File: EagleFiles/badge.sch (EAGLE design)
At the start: 8 parts, among them Q1 16MHz, U1 ATMEGA328P_TQFP

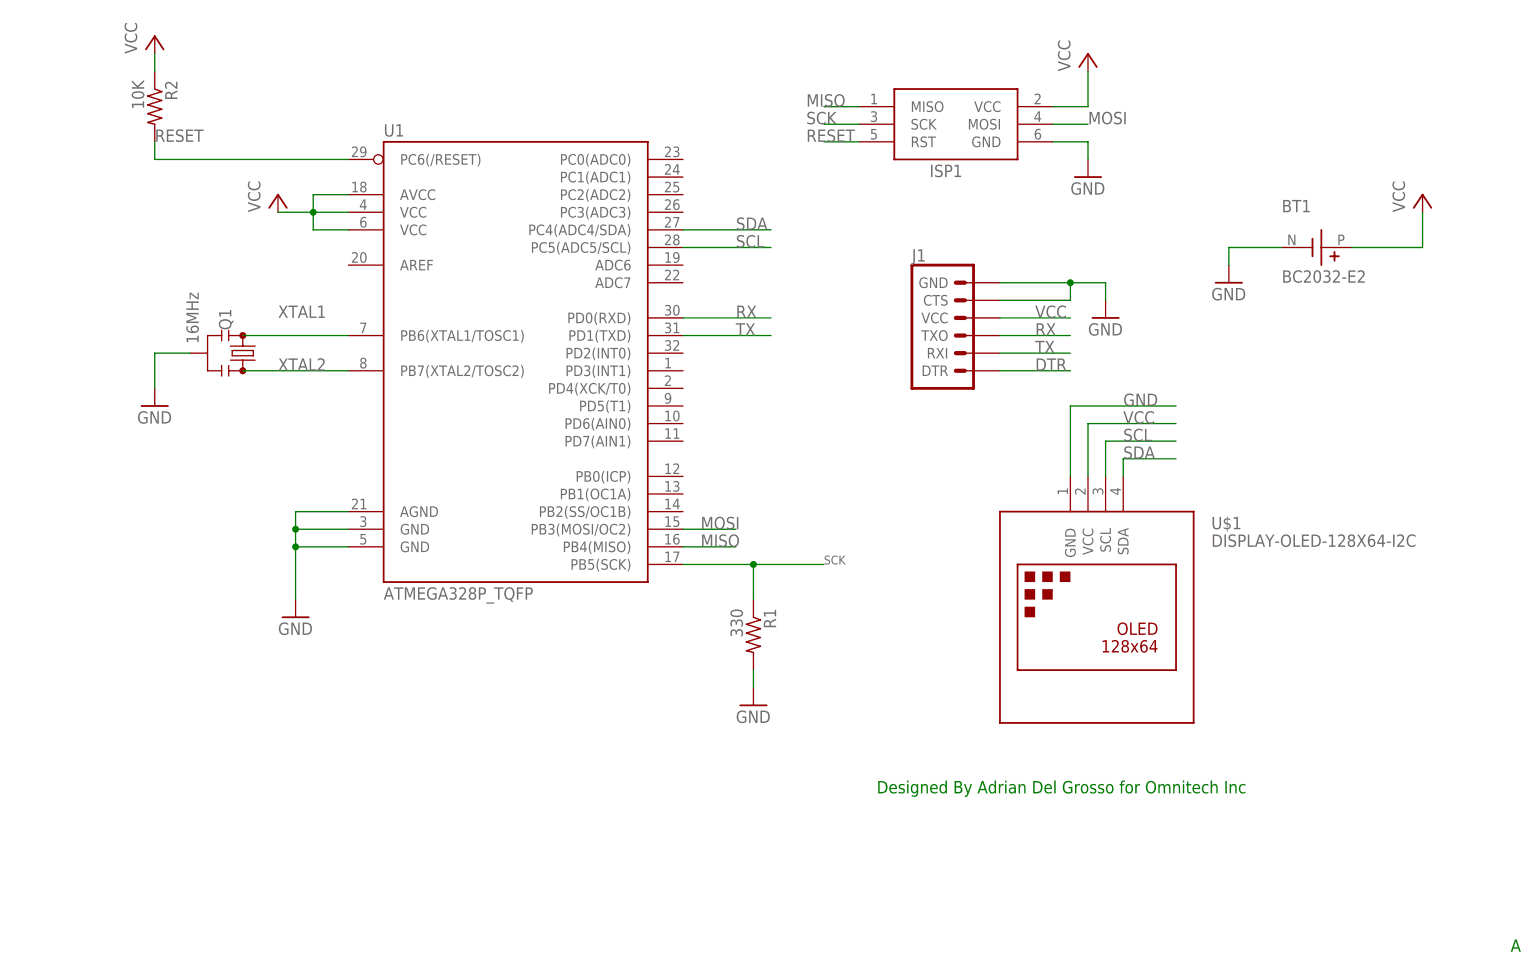
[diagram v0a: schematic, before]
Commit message: Added screen documentation, updated Eagle Files, added starter Arduino sketch
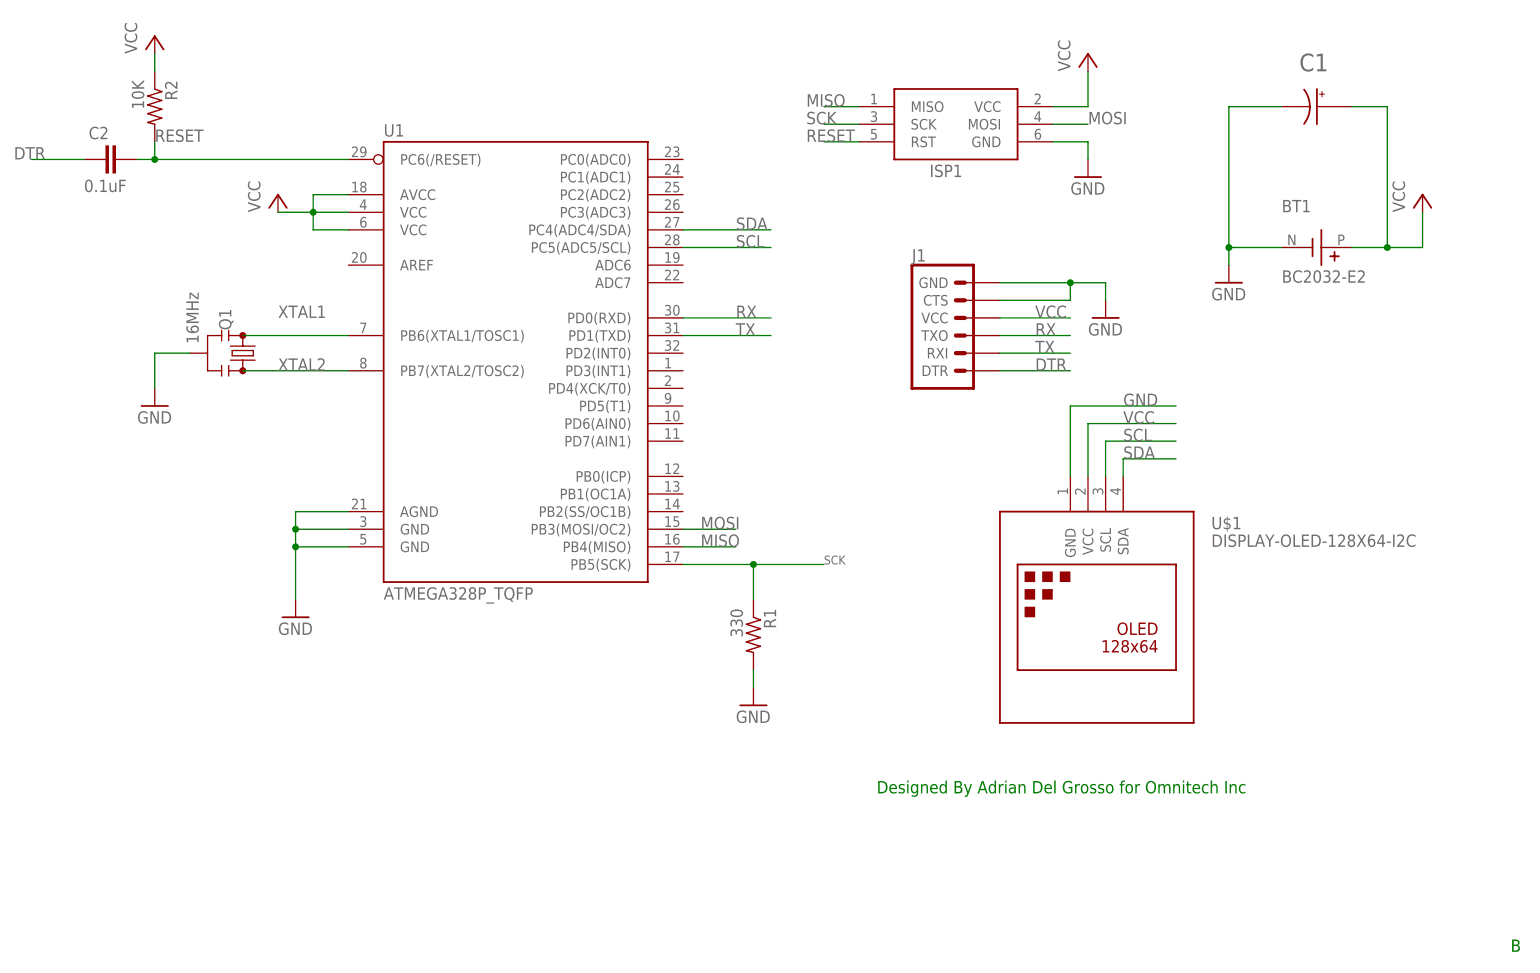
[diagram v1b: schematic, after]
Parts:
- added C1: RNE1C101MDS1PX, RNE1C101MDS1PX:RNE1C101MDS1PX
- added C2: 0.1uF, SparkFun-Capacitors:0.1UF-0402-16V-10%
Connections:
- net DTR: now also C2.1
- net GND: now also C1.N
- net RESET: now also C2.2
- net VCC: now also C1.P
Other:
- note added: "B"
- note removed: "A"
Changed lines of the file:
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@@
 <part name="GND6" library="supply1" library_urn="urn:adsk.eagle:library:371" deviceset="GND" device=""/>
 <part name="P+4" library="supply1" library_urn="urn:adsk.eagle:library:371" deviceset="VCC" device=""/>
+<part name="C1" library="RNE1C101MDS1PX" deviceset="RNE1C101MDS1PX" device=""/>
+<part name="C2" library="SparkFun-Capacitors" library_urn="urn:adsk.eagle:library:510" deviceset="0.1UF" device="-0402-16V-10%" package3d_urn="urn:adsk.eagle:package:37413/1" value="0.1uF"/>
 </parts>
 <sheets>
@@
 <plain>
 <text x="109.22" y="-7.62" size="1.778" layer="91">Designed By Adrian Del Grosso for Omnitech Inc</text>
-<text x="200.66" y="-30.48" size="1.778" layer="91">A</text>
+<text x="200.66" y="-30.48" size="1.778" layer="91">B</text>
 </plain>
 <instances>
@@
 <attribute name="VALUE" x="185.42" y="76.2" size="1.778" layer="96" rot="R90"/>
 </instance>
+<instance part="C1" gate="G$1" x="172.72" y="91.44" smashed="yes" rot="R270">
+<attribute name="NAME" x="170.17371875" y="96.5326" size="2.543140625" layer="95"/>
+</instance>
+<instance part="C2" gate="G$1" x="0" y="83.82" smashed="yes" rot="R90">
+<attribute name="NAME" x="-1.524" y="88.519" size="1.778" layer="95" font="vector" rot="R180"/>
+<attribute name="VALUE" x="1.016" y="80.899" size="1.778" layer="96" font="vector" rot="R180"/>
+</instance>
 </instances>
 <busses>
@@
 <wire x1="5.08" y1="86.36" x2="5.08" y2="83.82" width="0.1524" layer="91"/>
 <label x="5.08" y="86.36" size="1.778" layer="95"/>
+<wire x1="2.54" y1="83.82" x2="5.08" y2="83.82" width="0.1524" layer="91"/>
+<junction x="5.08" y="83.82"/>
+<pinref part="C2" gate="G$1" pin="2"/>
 </segment>
 <segment>
@@
 <wire x1="160.02" y1="71.12" x2="160.02" y2="68.58" width="0.1524" layer="91"/>
 <pinref part="GND6" gate="1" pin="GND"/>
+<wire x1="160.02" y1="91.44" x2="160.02" y2="71.12" width="0.1524" layer="91"/>
+<junction x="160.02" y="71.12"/>
+<pinref part="C1" gate="G$1" pin="N"/>
+<wire x1="160.02" y1="91.44" x2="167.64" y2="91.44" width="0.1524" layer="91"/>
 </segment>
 </net>
@@
 <segment>
 <pinref part="BT1" gate="G$1" pin="P"/>
-<wire x1="177.8" y1="71.12" x2="187.96" y2="71.12" width="0.1524" layer="91"/>
+<wire x1="177.8" y1="71.12" x2="182.88" y2="71.12" width="0.1524" layer="91"/>
+<wire x1="182.88" y1="71.12" x2="187.96" y2="71.12" width="0.1524" layer="91"/>
 <wire x1="187.96" y1="71.12" x2="187.96" y2="76.2" width="0.1524" layer="91"/>
 <pinref part="P+4" gate="VCC" pin="VCC"/>
+<wire x1="182.88" y1="91.44" x2="182.88" y2="71.12" width="0.1524" layer="91"/>
+<junction x="182.88" y="71.12"/>
+<pinref part="C1" gate="G$1" pin="P"/>
+<wire x1="177.8" y1="91.44" x2="182.88" y2="91.44" width="0.1524" layer="91"/>
 </segment>
 </net>
@@
 <label x="132.08" y="53.34" size="1.778" layer="95"/>
 </segment>
-</net>
+<segment>
+<wire x1="-5.08" y1="83.82" x2="-12.7" y2="83.82" width="0.1524" layer="91"/>
+<label x="-15.24" y="83.82" size="1.778" layer="95"/>
+<pinref part="C2" gate="G$1" pin="1"/>
+</segment>
+</net>
